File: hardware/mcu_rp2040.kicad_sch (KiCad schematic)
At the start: 30 parts, among them SW1 PTS815 SJM 250 SMTR LFS, U1 RP2040, U2 W25Q128JVSIQ, X1 ABM8AIG-12.000MHZ-12-2Z-T3

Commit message: Added digikey part numbers; usb trace width update
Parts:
- C1, C12, C14, C15, C2, C6, C7, C8, C9: Digikey Part Number (none) -> 1276-1857-1-ND
- C10, C11: Digikey Part Number (none) -> 1276-1296-1-ND
- C13, C3, C4, C5: Digikey Part Number (none) -> 1276-2955-1-ND
- R2: Digikey Part Number (none) -> P200CCT-ND
- R3, R4: Digikey Part Number (none) -> P27.0HCT-ND
- R5, R6: Digikey Part Number (none) -> A102203CT-ND
- R7: Digikey Part Number (none) -> P1.0DCT-ND
- R8, R9: Digikey Part Number (none) -> A102226CT-ND
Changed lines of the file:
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@@
 			)
 		)
+		(property "Digikey Part Number" "1276-1857-1-ND"
+			(at 71.12 160.02 0)
+			(effects
+				(font
+					(size 1.27 1.27)
+				)
+				(hide yes)
+			)
+		)
 		(pin "1"
 		)
@@
 			)
 		)
+		(property "Digikey Part Number" "A102226CT-ND"
+			(at 40.64 152.4 90)
+			(effects
+				(font
+					(size 1.27 1.27)
+				)
+				(hide yes)
+			)
+		)
 		(pin "2"
 		)
@@
 			)
 		)
+		(property "Digikey Part Number" "1276-2955-1-ND"
+			(at 185.42 57.15 0)
+			(effects
+				(font
+					(size 1.27 1.27)
+				)
+				(hide yes)
+			)
+		)
 		(pin "1"
 		)
@@
 			)
 		)
+		(property "Digikey Part Number" "1276-1857-1-ND"
+			(at 86.36 114.3 0)
+			(effects
+				(font
+					(size 1.27 1.27)
+				)
+				(hide yes)
+			)
+		)
 		(pin "1"
 		)
@@
 			)
 		)
+		(property "Digikey Part Number" "1276-1857-1-ND"
+			(at 138.43 170.18 0)
+			(effects
+				(font
+					(size 1.27 1.27)
+				)
+				(hide yes)
+			)
+		)
 		(pin "1"
 		)
@@
 			)
 		)
+		(property "Digikey Part Number" "1276-2955-1-ND"
+			(at 82.55 160.02 0)
+			(effects
+				(font
+					(size 1.27 1.27)
+				)
+				(hide yes)
+			)
+		)
 		(pin "1"
 		)
@@
 			)
 		)
+		(property "Digikey Part Number" "P27.0HCT-ND"
+			(at 154.94 33.02 0)
+			(effects
+				(font
+					(size 1.27 1.27)
+				)
+				(hide yes)
+			)
+		)
 		(pin "2"
 		)
@@
 			)
 		)
+		(property "Digikey Part Number" "1276-1857-1-ND"
+			(at 113.03 54.61 0)
+			(effects
+				(font
+					(size 1.27 1.27)
+				)
+				(hide yes)
+			)
+		)
 		(pin "1"
 		)
@@
 			)
 		)
+		(property "Digikey Part Number" "P27.0HCT-ND"
+			(at 144.78 33.02 0)
+			(effects
+				(font
+					(size 1.27 1.27)
+				)
+				(hide yes)
+			)
+		)
 		(pin "2"
 		)
@@
 			)
 		)
+		(property "Digikey Part Number" "P1.0DCT-ND"
+			(at 185.42 40.64 0)
+			(effects
+				(font
+					(size 1.27 1.27)
+				)
+				(hide yes)
+			)
+		)
 		(pin "2"
 		)
@@
 			)
 		)
+		(property "Digikey Part Number" "A102226CT-ND"
+			(at 255.27 128.27 0)
+			(effects
+				(font
+					(size 1.27 1.27)
+				)
+				(hide yes)
+			)
+		)
 		(pin "2"
 		)
@@
 			)
 		)
+		(property "Digikey Part Number" "1276-1857-1-ND"
+			(at 203.2 115.57 0)
+			(effects
+				(font
+					(size 1.27 1.27)
+				)
+				(hide yes)
+			)
+		)
 		(pin "1"
 		)
@@
 			)
 		)
+		(property "Digikey Part Number" "1276-1296-1-ND"
+			(at 219.71 151.13 0)
+			(effects
+				(font
+					(size 1.27 1.27)
+				)
+				(hide yes)
+			)
+		)
 		(pin "1"
 		)
@@
 			)
 		)
+		(property "Digikey Part Number" "1276-1857-1-ND"
+			(at 151.13 170.18 0)
+			(effects
+				(font
+					(size 1.27 1.27)
+				)
+				(hide yes)
+			)
+		)
 		(pin "1"
 		)
@@
 			)
 		)
+		(property "Digikey Part Number" "1276-1857-1-ND"
+			(at 101.6 54.61 0)
+			(effects
+				(font
+					(size 1.27 1.27)
+				)
+				(hide yes)
+			)
+		)
 		(pin "1"
 		)
@@
 			)
 		)
+		(property "Digikey Part Number" "1276-1857-1-ND"
+			(at 203.2 93.98 0)
+			(effects
+				(font
+					(size 1.27 1.27)
+				)
+				(hide yes)
+			)
+		)
 		(pin "1"
 		)
@@
 			)
 		)
+		(property "Digikey Part Number" "1276-2955-1-ND"
+			(at 162.56 57.15 0)
+			(effects
+				(font
+					(size 1.27 1.27)
+				)
+				(hide yes)
+			)
+		)
 		(pin "1"
 		)
@@
 			)
 		)
+		(property "Digikey Part Number" "1276-2955-1-ND"
+			(at 172.72 57.15 0)
+			(effects
+				(font
+					(size 1.27 1.27)
+				)
+				(hide yes)
+			)
+		)
 		(pin "1"
 		)
@@
 			)
 		)
+		(property "Digikey Part Number" "A102203CT-ND"
+			(at 36.83 38.1 0)
+			(effects
+				(font
+					(size 1.27 1.27)
+				)
+				(hide yes)
+			)
+		)
 		(pin "2"
 		)
@@
 			)
 		)
+		(property "Digikey Part Number" "1276-1857-1-ND"
+			(at 86.36 90.17 0)
+			(effects
+				(font
+					(size 1.27 1.27)
+				)
+				(hide yes)
+			)
+		)
 		(pin "1"
 		)
@@
 			)
 		)
+		(property "Digikey Part Number" "1276-1296-1-ND"
+			(at 255.27 151.13 0)
+			(effects
+				(font
+					(size 1.27 1.27)
+				)
+				(hide yes)
+			)
+		)
 		(pin "1"
 		)
@@
 			)
 		)
+		(property "Digikey Part Number" "P200CCT-ND"
+			(at 185.42 27.94 0)
+			(effects
+				(font
+					(size 1.27 1.27)
+				)
+				(hide yes)
+			)
+		)
 		(pin "2"
 		)
@@
 			)
 		)
+		(property "Digikey Part Number" "A102203CT-ND"
+			(at 26.67 38.1 0)
+			(effects
+				(font
+					(size 1.27 1.27)
+				)
+				(hide yes)
+			)
+		)

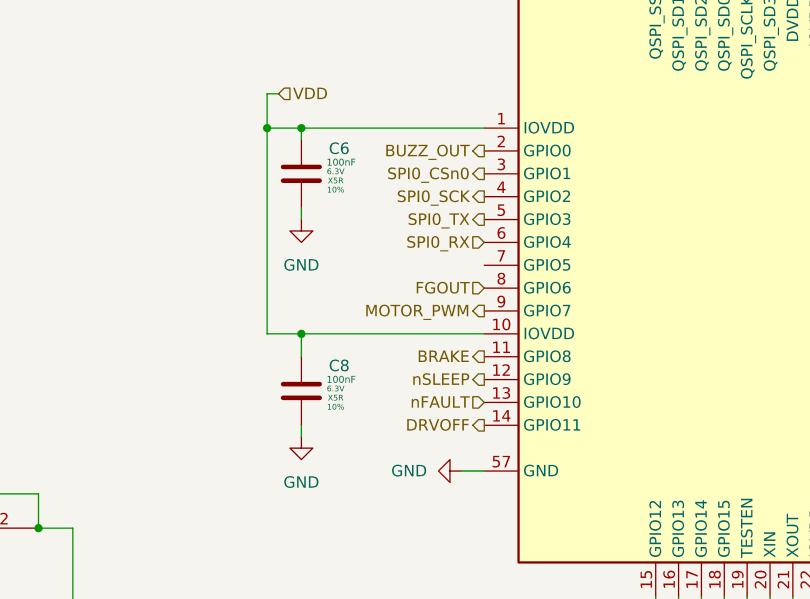
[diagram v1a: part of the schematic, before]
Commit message: Rev 2 of Custom PCB but without Motor Driver (Replaced with Optocoupler Circuit for Standard Servo) (#15)
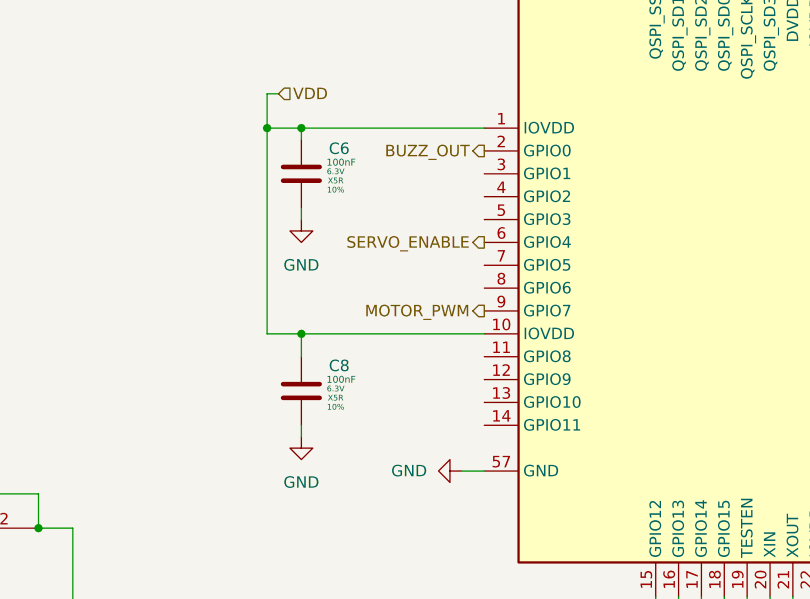
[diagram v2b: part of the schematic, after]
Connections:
- net BRAKE: no longer names the net of U1.11 (GPIO8)
- net DRVOFF: no longer names the net of U1.14 (GPIO11)
- net FGOUT: no longer names the net of U1.8 (GPIO6)
- net SPI0_CSn0: no longer names the net of U1.3 (GPIO1)
- net SPI0_RX renamed SERVO_ENABLE
- net SPI0_SCK: no longer names the net of U1.4 (GPIO2)
- net SPI0_TX: no longer names the net of U1.5 (GPIO3)
- net nFAULT: no longer names the net of U1.13 (GPIO10)
- net nSLEEP: no longer names the net of U1.12 (GPIO9)
